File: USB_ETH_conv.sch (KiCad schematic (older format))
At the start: 35 parts, among them J3 RJ45-TRANSFO, U4 LAN9500A, Y2 25MHz

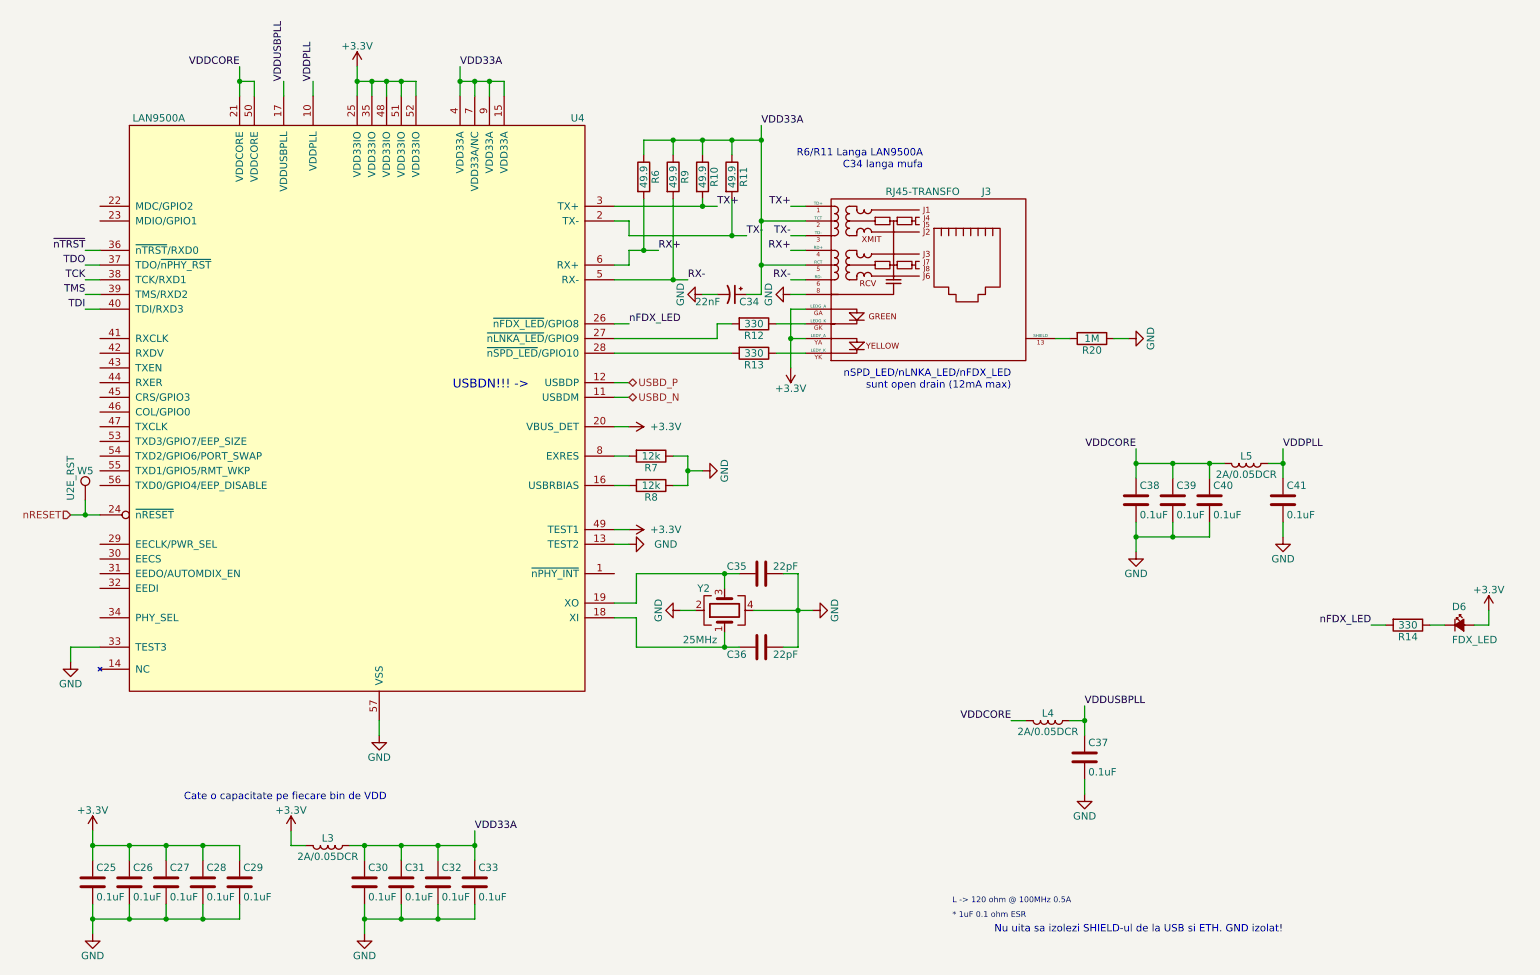
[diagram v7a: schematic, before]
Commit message: Finished first version of PCB.
Modified RJ45 footprint.
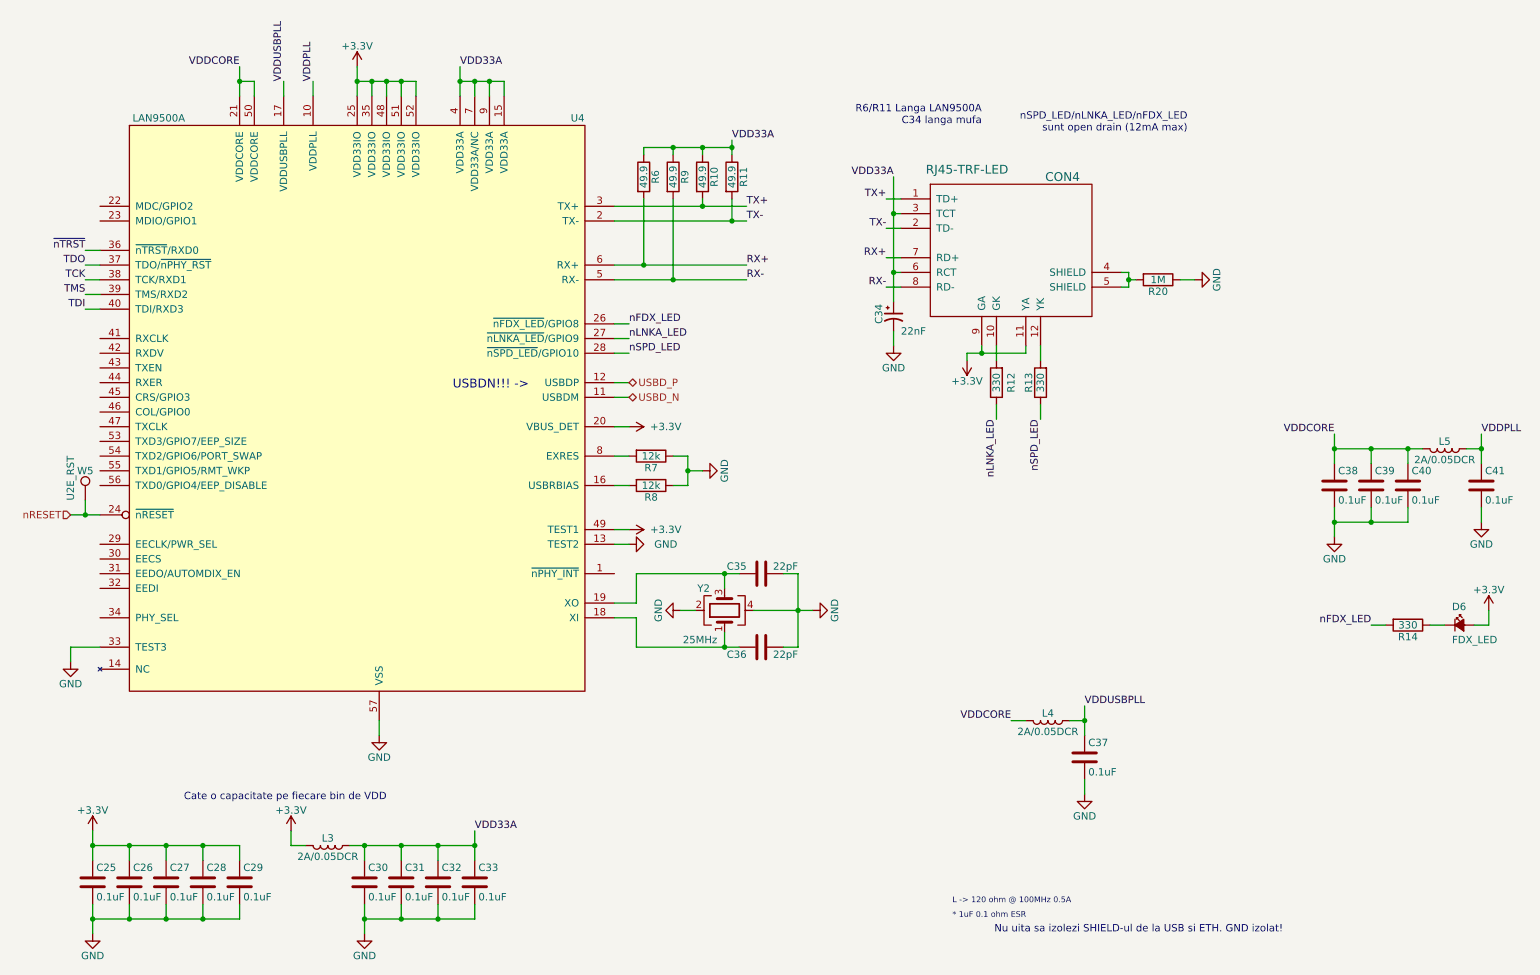
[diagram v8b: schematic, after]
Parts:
- removed J3: RJ45-TRANSFO, Connectors:RJ45_TRANSFO, symbol RJ45-TRANSFO
- added CON4: RJ45-TRF-LED, misc:RJ45_TRANSFO, symbol RJ45-TRF-LED
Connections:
- net +3V3: now also CON4.11 (YA), CON4.9 (GA)
- net RX+: now also CON4.7 (RD+)
- net RX-: now also CON4.8 (RD-)
- net TX+: now also CON4.1 (TD+)
- net TX-: now also CON4.2 (TD-)
- net VDD33A: now also CON4.3 (TCT), CON4.6 (RCT)
- net at R12.2: now also CON4.10 (GK); no longer U4.27 (~nLNKA_LED~/GPIO9)
- net at R13.2: now also CON4.12 (YK); no longer U4.28 (~nSPD_LED~/GPIO10)
- net at R20.2: now also CON4.4 (SHIELD), CON4.5 (SHIELD)
- net nLNKA_LED: now reaches R12.1
- net nLNKA_LED: now also U4.27 (~nLNKA_LED~/GPIO9)
- net nSPD_LED: now reaches R13.1
- net nSPD_LED: now also U4.28 (~nSPD_LED~/GPIO10)
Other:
- moved on the sheet: C34, C38, C39, C40, C41, L5, R12, R13, R20
